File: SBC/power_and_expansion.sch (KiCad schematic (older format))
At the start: 18 parts, among them J1 VCC1, J10 GND3, J11 Expansion Bus, J2 GND1, J3 VCC2, J4 POWER, J5 GND2, J9 VCC3

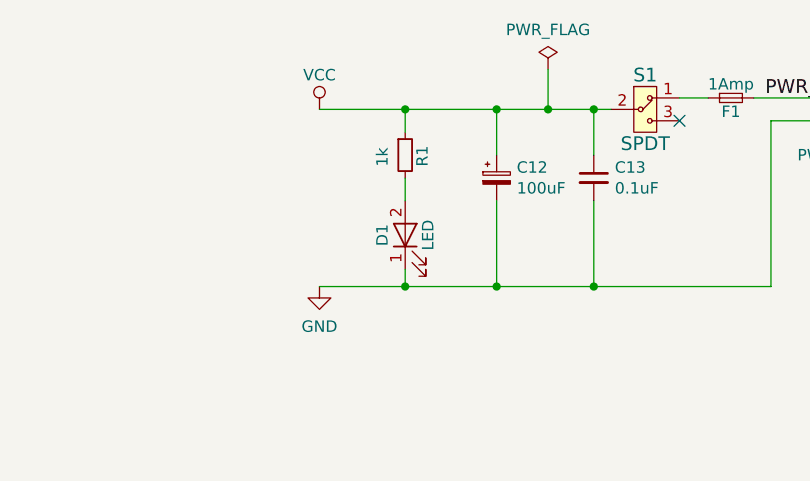
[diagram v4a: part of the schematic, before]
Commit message: Added de-coupling cap to 74hc74. Rearranged PCB a bit.
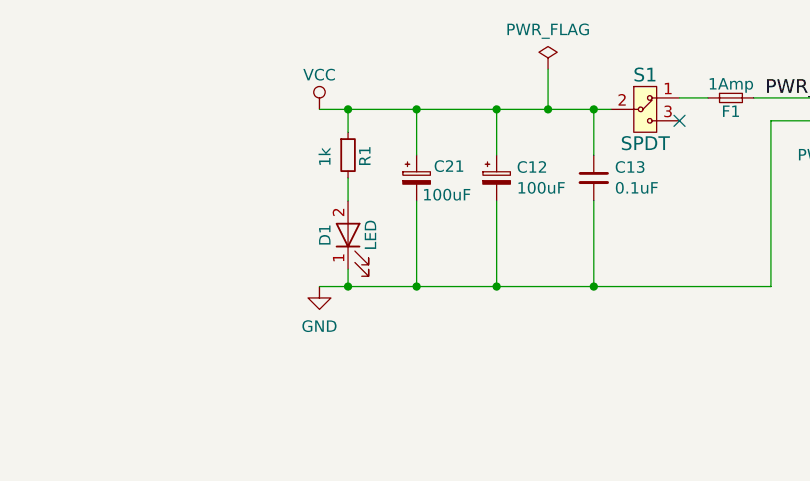
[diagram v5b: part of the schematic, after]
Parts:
- added C21: 100uF, Capacitor_Tantalum_SMD:CP_EIA-3528-15_AVX-H_Pad1.50x2.35mm_HandSolder, symbol Device:CP_Small
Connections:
- net GND: now also C21.2
- net VCC: now also C21.1
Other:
- moved on the sheet: D1, R1
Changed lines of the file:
@@
 L pluto-rescue:LED D1
 U 1 1 5A30C5EA
-P 5375 2175
-F 0 "D1" H 5375 2275 50  0000 C CNN
-F 1 "LED" H 5375 2075 50  0000 C CNN
-F 2 "LEDs:LED_D3.0mm" H 5375 2175 50  0001 C CNN
-F 3 "" H 5375 2175 50  0001 C CNN
-	1    5375 2175
+P 5125 2175
+F 0 "D1" H 5125 2275 50  0000 C CNN
+F 1 "LED" H 5125 2075 50  0000 C CNN
+F 2 "LEDs:LED_D3.0mm" H 5125 2175 50  0001 C CNN
+F 3 "" H 5125 2175 50  0001 C CNN
+	1    5125 2175
 	0    -1   -1   0
 $EndComp
@@
 L pluto-rescue:R_Small-device R1
 U 1 1 5A30C649
-P 5375 1825
-F 0 "R1" V 5450 1775 50  0000 L CNN
-F 1 "1k" V 5275 1775 50  0000 L CNN
-F 2 "Resistor_SMD:R_1206_3216Metric_Pad1.42x1.75mm_HandSolder" H 5375 1825 50  0001 C CNN
-F 3 "" H 5375 1825 50  0001 C CNN
-	1    5375 1825
+P 5125 1825
+F 0 "R1" V 5200 1775 50  0000 L CNN
+F 1 "1k" V 5025 1775 50  0000 L CNN
+F 2 "Resistor_SMD:R_1206_3216Metric_Pad1.42x1.75mm_HandSolder" H 5125 1825 50  0001 C CNN
+F 3 "" H 5125 1825 50  0001 C CNN
+	1    5125 1825
 	1    0    0    -1
 $EndComp
@@
 Connection ~ 5775 1625
 Wire Wire Line
-	5775 1625 5375 1625
-Wire Wire Line
 	5775 2025 5775 2400
 Wire Wire Line
@@
 Connection ~ 5775 2400
 Wire Wire Line
-	5775 2400 5375 2400
-Wire Wire Line
-	5375 1725 5375 1625
-Connection ~ 5375 1625
-Wire Wire Line
-	5375 1625 5000 1625
-Wire Wire Line
-	5375 1925 5375 2025
-Wire Wire Line
-	5375 2325 5375 2400
+	5125 1725 5125 1625
+Wire Wire Line
+	5125 1925 5125 2025
+$Comp
+L Device:CP_Small C21
+U 1 1 5D9894B8
+P 5425 1925
+F 0 "C21" H 5500 1975 50  0000 L CNN
+F 1 "100uF" H 5450 1850 50  0000 L CNN
+F 2 "Capacitor_Tantalum_SMD:CP_EIA-3528-15_AVX-H_Pad1.50x2.35mm_HandSolder" H 5425 1925 50  0001 C CNN
+F 3 "~" H 5425 1925 50  0001 C CNN
+	1    5425 1925
+	1    0    0    -1
+$EndComp
+Connection ~ 5125 1625
+Wire Wire Line
+	5125 1625 5000 1625
+Wire Wire Line
+	5000 2400 5125 2400
+Wire Wire Line
+	5125 2325 5125 2400
+Connection ~ 5125 2400
+Wire Wire Line
+	5125 2400 5425 2400
+Wire Wire Line
+	5125 1625 5425 1625
+Wire Wire Line
+	5425 1625 5425 1825
 Wire Bus Line
 	9500 3175 9500 3875
 Wire Bus Line
 	8000 3175 8000 4675
-Connection ~ 5375 2400
-Wire Wire Line
-	5375 2400 5000 2400
+Wire Wire Line
+	5425 2025 5425 2400
+Connection ~ 5425 1625
+Wire Wire Line
+	5425 1625 5775 1625
+Connection ~ 5425 2400
+Wire Wire Line
+	5425 2400 5775 2400
 $EndSCHEMATC
